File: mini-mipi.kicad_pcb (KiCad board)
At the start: 4 copper layers, 43.2 x 34.9 mm, 56 parts, among them IC1 ECP5-BGA256, J1 Conn_ARM_JTAG_SWD_10, J2 Conn_01x15, J3 USB_B_Micro, J4 Micro_SD_Card, U1 TPS74633, U2 TPS74618, U3 TPS74625, U4 TPS74611, U5 AT25SF081-SSHD-X, U6 S27KL0641, U7 OSC_25M

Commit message: Add semi-critical resistor values
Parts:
- R1, R2, R3: value R -> 10k
- R12, R13, R14, R15, R17, R18: value R -> 4.7k
- R16: value R -> 1k
- R6: value R -> 15k
- R7, R8: value R_Small -> 0
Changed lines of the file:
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@@
-(kicad_pcb (version 20200628) (host pcbnew "5.99.0-unknown-7340c97~102~ubuntu20.04.1")
+(kicad_pcb (version 20200628) (host pcbnew "5.99.0-unknown-e9da02e~102~ubuntu20.04.1")
   (general
     (thickness 1.6)
@@
       (effects (font (size 1 1) (thickness 0.15)))
     )
-    (fp_text value "R" (at 0 1.17) (layer "F.Fab")
+    (fp_text value "4.7k" (at 0 1.17) (layer "F.Fab")
       (effects (font (size 1 1) (thickness 0.15)))
     )
@@
       (effects (font (size 1 1) (thickness 0.15)) (justify mirror))
     )
-    (fp_text value "R" (at 0 -1.17) (layer "B.Fab")
+    (fp_text value "4.7k" (at 0 -1.17) (layer "B.Fab")
       (effects (font (size 1 1) (thickness 0.15)) (justify mirror))
     )
@@
       (effects (font (size 1 1) (thickness 0.15)) (justify mirror))
     )
-    (fp_text value "R" (at 0 -1.17) (layer "B.Fab")
+    (fp_text value "1k" (at 0 -1.17) (layer "B.Fab")
       (effects (font (size 1 1) (thickness 0.15)) (justify mirror))
     )
@@
       (effects (font (size 1 1) (thickness 0.15)) (justify mirror))
     )
-    (fp_text value "R" (at 0 -1.17) (layer "B.Fab")
+    (fp_text value "4.7k" (at 0 -1.17) (layer "B.Fab")
       (effects (font (size 1 1) (thickness 0.15)) (justify mirror))
     )
@@
       (effects (font (size 1 1) (thickness 0.15)) (justify mirror))
     )
-    (fp_text value "R" (at 0 -1.17) (layer "B.Fab")
+    (fp_text value "4.7k" (at 0 -1.17) (layer "B.Fab")
       (effects (font (size 1 1) (thickness 0.15)) (justify mirror))
     )
@@
       (effects (font (size 1 1) (thickness 0.15)) (justify mirror))
     )
-    (fp_text value "R" (at 0 -1.17) (layer "B.Fab")
+    (fp_text value "4.7k" (at 0 -1.17) (layer "B.Fab")
       (effects (font (size 1 1) (thickness 0.15)) (justify mirror))
     )
@@
       (effects (font (size 1 1) (thickness 0.15)) (justify mirror))
     )
-    (fp_text value "R" (at 0 -1.17) (layer "B.Fab")
+    (fp_text value "4.7k" (at 0 -1.17) (layer "B.Fab")
       (effects (font (size 1 1) (thickness 0.15)) (justify mirror))
     )
@@
       (effects (font (size 1 1) (thickness 0.15)))
     )
-    (fp_text value "R_Small" (at 0 1.17 90) (layer "F.Fab")
+    (fp_text value "0" (at 0 1.17 90) (layer "F.Fab")
       (effects (font (size 1 1) (thickness 0.15)))
     )
@@
       (effects (font (size 1 1) (thickness 0.15)))
     )
-    (fp_text value "R_Small" (at 0 1.17 90) (layer "F.Fab")
+    (fp_text value "0" (at 0 1.17 90) (layer "F.Fab")
       (effects (font (size 1 1) (thickness 0.15)))
     )
@@
       (effects (font (size 1 1) (thickness 0.15)))
     )
-    (fp_text value "R" (at 0 1.17 90) (layer "F.Fab")
+    (fp_text value "15k" (at 0 1.17 90) (layer "F.Fab")
       (effects (font (size 1 1) (thickness 0.15)))
     )
@@
       (effects (font (size 1 1) (thickness 0.15)) (justify mirror))
     )
-    (fp_text value "R" (at 0 -1.17 90) (layer "B.Fab")
+    (fp_text value "10k" (at 0 -1.17 90) (layer "B.Fab")
       (effects (font (size 1 1) (thickness 0.15)) (justify mirror))
     )
@@
       (effects (font (size 1 1) (thickness 0.15)) (justify mirror))
     )
-    (fp_text value "R" (at 0 -1.17 90) (layer "B.Fab")
+    (fp_text value "10k" (at 0 -1.17 90) (layer "B.Fab")
       (effects (font (size 1 1) (thickness 0.15)) (justify mirror))
     )
@@
       (effects (font (size 1 1) (thickness 0.15)) (justify mirror))
     )
-    (fp_text value "R" (at 0 -1.17 90) (layer "B.Fab")
-      (effects (font (size 1 1) (thickness 0.15)) (justify mirror))
-    )
+    (fp_text value "10k" (at 0 -1.17 90) (layer "B.Fab")
+      (effects (font (size 1 1) (thickness 0.15)) (justify mirror))
+    )

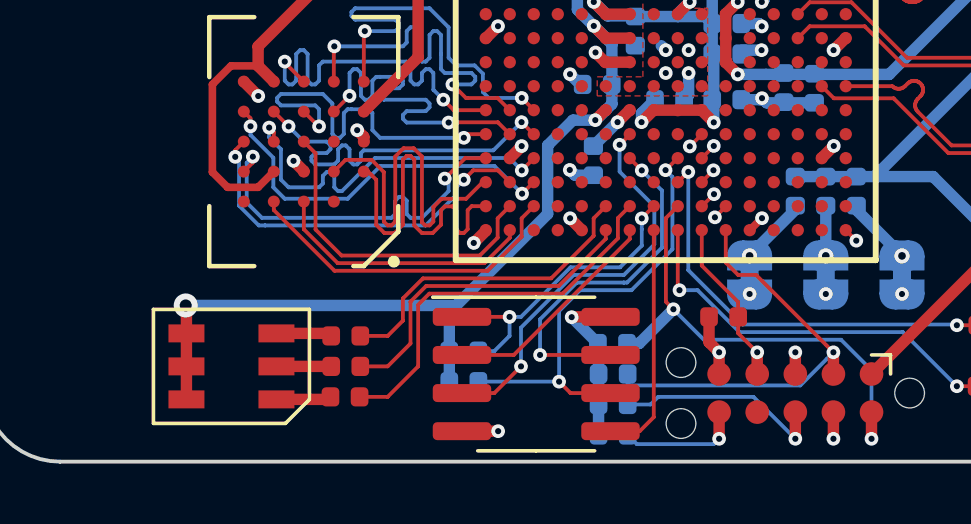
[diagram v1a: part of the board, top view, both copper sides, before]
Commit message: Add more pullup resistors
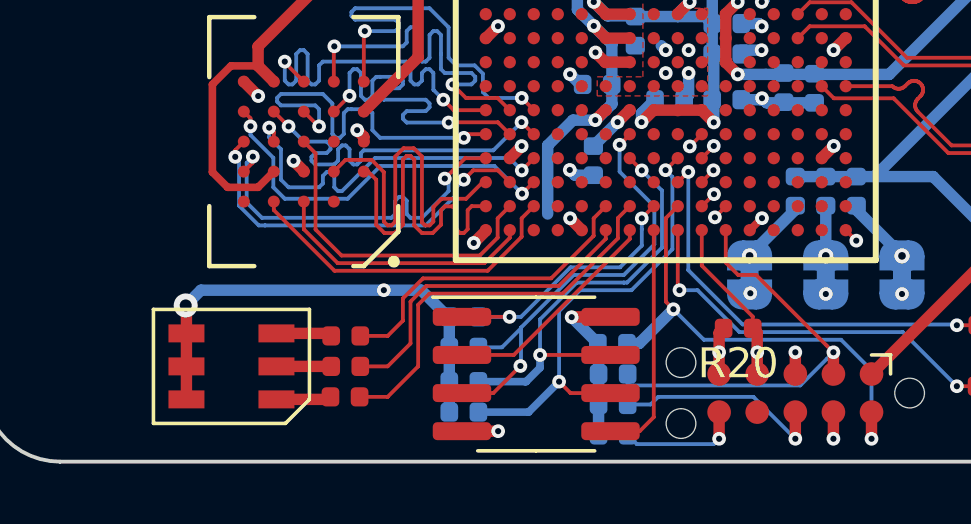
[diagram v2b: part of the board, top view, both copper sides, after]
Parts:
- added R19: 4.7k, Resistor_SMD:R_0402_1005Metric, B.Cu at (157.6, 94.5)
- added R20: 4.7k, Resistor_SMD:R_0402_1005Metric, F.Cu at (166.8, 92.7)
- R18: moved to B.Cu
- moved R18 8.72 mm to (157.6, 93.3)
- moved R17 1.14 mm to (157.6, 92.3)
- moved R16 1.02 mm to (157.6, 95.5)
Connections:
- R18 pad 1: GND -> VCC
- R18 pad 2: /CONFIG/TCK -> /CONFIG/DIO2
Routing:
- net VCC: track 127.6 -> 130.8 mm, vias 14 -> 15
- net /CONFIG/DIO3: track 12.0 -> 14.7 mm
- net /CONFIG/DIO2: track 13.5 -> 15.2 mm
- net /CONFIG/CSN: track 10.3 -> 9.50 mm

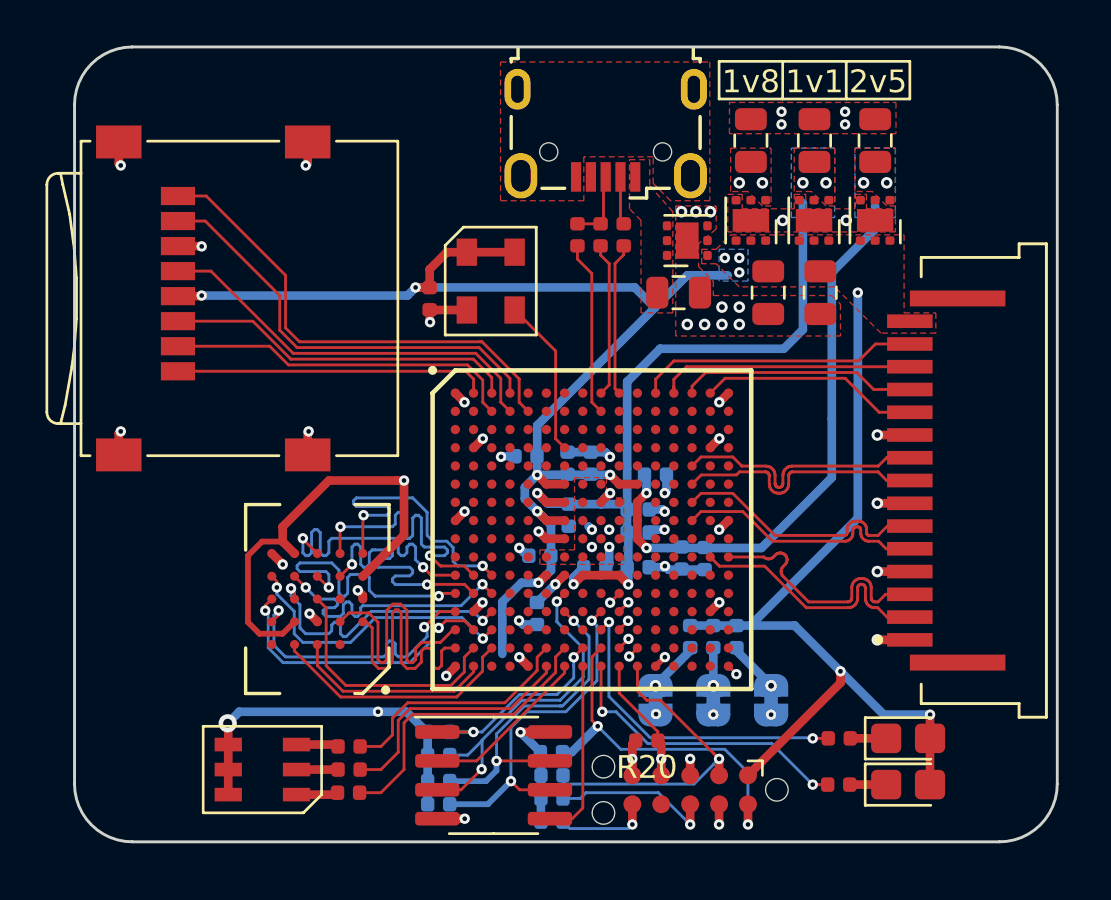
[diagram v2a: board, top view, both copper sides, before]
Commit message: Change oscillator to SI5315, change RGB LED
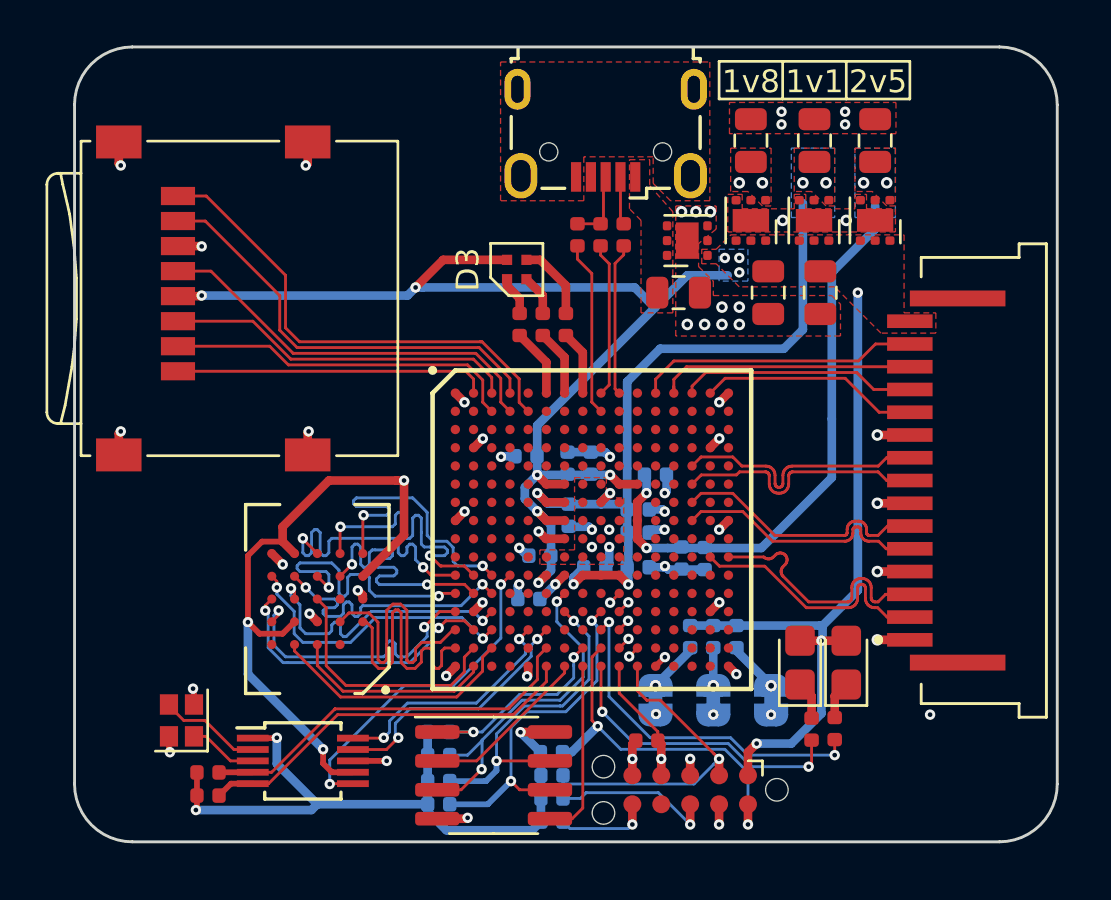
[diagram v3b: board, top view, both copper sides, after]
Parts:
- removed C1: C, Capacitor_SMD:C_0402_1005Metric
- added R21: R, Resistor_SMD:R_0402_1005Metric, F.Cu at (147.5, 94.1)
- added R22: R, Resistor_SMD:R_0402_1005Metric, F.Cu at (147.5, 95.1)
- added Y1: Crystal_GND24, Crystal:Crystal_SMD_2016-4Pin_2.0x1.6mm, F.Cu at (146.3, 91.8)
- D3: value LED_RGB -> LED_RGBA; footprint mini-mipi:FM-Z3535RGBA-SH -> mini-mipi:LED_0404
- U7: value OSC_25M -> SI5351A-B-GTR; footprint mini-mipi:SOIC-4 -> Package_SO:MSOP-10_3x3mm_P0.5mm
- moved D3 24.7 mm to (161.0, 72.0), turned to 0 degrees
- moved R11 22.7 mm to (163.2, 74.4), turned to -90 degrees
- moved U7 22.6 mm to (151.6, 93.6), turned to 0 degrees
- moved R10 21.3 mm to (162.2, 74.4), turned to -90 degrees
- moved R9 20.0 mm to (161.2, 74.4), turned to -90 degrees
- moved D1 7.16 mm to (173.5, 89.3), turned to 90 degrees
- moved D2 4.30 mm to (175.5, 89.3), turned to 90 degrees
- moved R4 2.71 mm to (174.0, 92.2), turned to 90 degrees
- moved C14 0.73 mm to (161.6, 86.5), turned to 180 degrees
- moved R5 0.47 mm to (175.0, 92.2), turned to 90 degrees
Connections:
- IC1 pad B1: Net-(IC1-PadB1) -> (no net)
- IC1 pad B2: Net-(IC1-PadB2) -> (no net)
- IC1 pad C1: Net-(IC1-PadC1) -> (no net)
- IC1 pad C2: Net-(IC1-PadC2) -> (no net)
- IC1 pad C3: Net-(IC1-PadC3) -> (no net)
- IC1 pad D1: Net-(IC1-PadD1) -> (no net)
- IC1 pad D3: Net-(IC1-PadD3) -> (no net)
- IC1 pad E1: Net-(IC1-PadE1) -> (no net)
- IC1 pad E2: Net-(IC1-PadE2) -> (no net)
- IC1 pad E3: Net-(IC1-PadE3) -> (no net)
- IC1 pad F1: Net-(IC1-PadF1) -> (no net)
- IC1 pad F2: Net-(IC1-PadF2) -> (no net)
- IC1 pad F3: Net-(IC1-PadF3) -> (no net)
- IC1 pad F4: Net-(IC1-PadF4) -> (no net)
- IC1 pad F5: Net-(IC1-PadF5) -> (no net)
- IC1 pad G1: Net-(IC1-PadG1) -> (no net)
- IC1 pad G2: Net-(IC1-PadG2) -> (no net)
- IC1 pad G3: Net-(IC1-PadG3) -> (no net)
- IC1 pad G4: Net-(IC1-PadG4) -> (no net)
- IC1 pad G5: Net-(IC1-PadG5) -> (no net)
- IC1 pad H2: Net-(IC1-PadH2) -> (no net)
- IC1 pad H3: Net-(IC1-PadH3) -> (no net)
- IC1 pad H4: Net-(IC1-PadH4) -> (no net)
- IC1 pad H5: Net-(IC1-PadH5) -> (no net)
- IC1 pad H6: VCC -> (no net)
- IC1 pad H7: VCC -> (no net)
- IC1 pad J1: Net-(IC1-PadJ1) -> (no net)
- IC1 pad J2: Net-(IC1-PadJ2) -> (no net)
- IC1 pad J3: Net-(IC1-PadJ3) -> (no net)
- IC1 pad J4: Net-(IC1-PadJ4) -> (no net)
- IC1 pad J5: Net-(IC1-PadJ5) -> (no net)
- IC1 pad K1: Net-(IC1-PadK1) -> (no net)
- IC1 pad K2: Net-(IC1-PadK2) -> (no net)
- IC1 pad K3: Net-(IC1-PadK3) -> (no net)
- IC1 pad R6: Net-(IC1-PadR6) -> OSC_SDA
- IC1 pad T6: Net-(IC1-PadT6) -> OSC_SCL
- R10 pad 2: Net-(IC1-PadT6) -> Net-(IC1-PadA7)
- R11 pad 1: Net-(D3-Pad1) -> Net-(D3-Pad3)
- R11 pad 2: Net-(IC1-PadR7) -> Net-(IC1-PadA8)
- R9 pad 1: Net-(D3-Pad3) -> Net-(D3-Pad1)
- R9 pad 2: Net-(IC1-PadR6) -> Net-(IC1-PadA6)
- U7 pad 2: GND -> /MEMORY/OSC_XA
- U7 pad 3: Net-(IC1-PadD7) -> /MEMORY/OSC_XB
- U7 pad 4: VCC -> OSC_SDA
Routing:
- net OSC_SDA: track 0.00 -> 17.2 mm
- net OSC_SCL: track 0.00 -> 17.1 mm
- net Net-(IC1-PadL4): track 0.00 -> 14.7 mm, vias 0 -> 2
- net Net-(IC1-PadR7): track 13.2 -> 0.00 mm
- net Net-(IC1-PadP6): track 0.00 -> 11.5 mm, vias 0 -> 2
- net Net-(IC1-PadT6): track 11.1 -> 0.00 mm
- net Net-(IC1-PadR6): track 10.8 -> 0.00 mm
- net Net-(IC1-PadP5): track 0.00 -> 10.7 mm, vias 0 -> 2
- net +1V8: track 50.1 -> 59.0 mm, vias 4 -> 6
- net VCC: track 130.8 -> 123.5 mm, vias 15 -> 16
- net Net-(IC1-PadD7): track 6.96 -> 0.00 mm
- net /MEMORY/OSC_XA: track 0.00 -> 4.53 mm
- net /MEMORY/OSC_XB: track 0.00 -> 3.03 mm
- net Net-(IC1-PadA6): track 0.00 -> 3.02 mm
- net Net-(IC1-PadA7): track 0.00 -> 2.93 mm
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
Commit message: Change 1.8v and 3.3v regulators to buck for #2
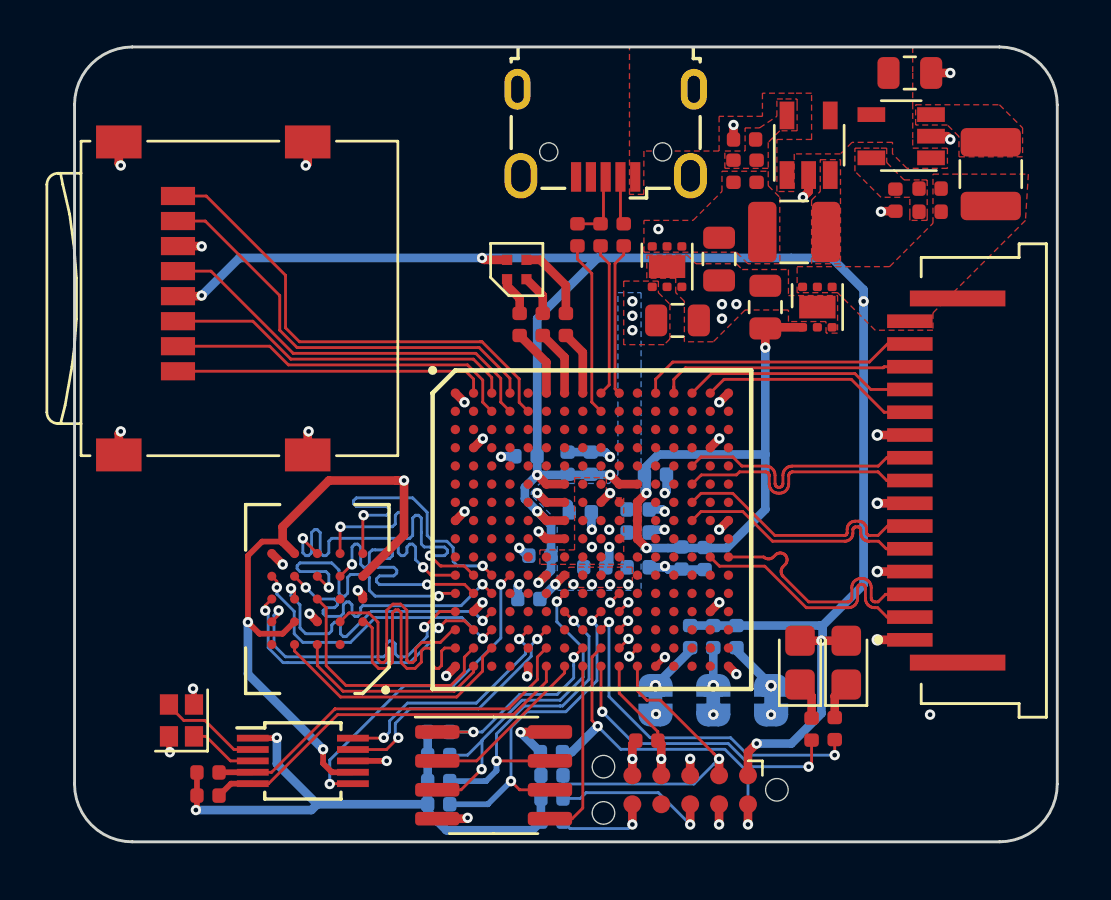
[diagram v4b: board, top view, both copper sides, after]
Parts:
- removed C2: C, Capacitor_SMD:C_0805_2012Metric
- added C21: C, Capacitor_SMD:C_0402_1005Metric, F.Cu at (170.6, 67.7)
- added L1: L, Inductor_SMD:L_1210_3225Metric, F.Cu at (181.9, 67.8)
- added L3: L, Inductor_SMD:L_1210_3225Metric, F.Cu at (173.2, 70.4)
- added R23: R, Resistor_SMD:R_0402_1005Metric, F.Cu at (179.2, 68.5)
- added R24: R, Resistor_SMD:R_0402_1005Metric, F.Cu at (177.7, 69.0)
- added R27: R, Resistor_SMD:R_0402_1005Metric, F.Cu at (171.6, 67.7)
- added R28: R, Resistor_SMD:R_0402_1005Metric, F.Cu at (171.0, 66.3)
- C4: footprint Capacitor_SMD:C_0805_2012Metric -> Capacitor_SMD:C_0402_1005Metric
- U1: value TPS74633 -> AP3429-A; footprint Package_SON:WSON-6-1EP_2x2mm_P0.65mm_EP1x1.6mm -> Package_TO_SOT_SMD:TSOT-23-5
- U2: value TPS74618 -> TPS74625
- U3: value TPS74625 -> AP3429-A; footprint Package_SON:WSON-6-1EP_2x2mm_P0.65mm_EP1x1.6mm -> Package_TO_SOT_SMD:TSOT-23-5
- moved U1 10.5 mm to (177.9, 66.2)
- moved C3 10.4 mm to (178.3, 63.4), turned to 0 degrees
- moved C8 9.93 mm to (168.1, 74.2), turned to 0 degrees
- moved C7 8.77 mm to (172.0, 73.7)
- moved C4 8.47 mm to (179.2, 69.5), turned to 180 degrees
- moved U4 6.77 mm to (167.6, 71.9), turned to 90 degrees
- moved U2 4.80 mm to (174.2, 73.7), turned to 90 degrees
- moved U3 4.41 mm to (173.9, 66.5), turned to 90 degrees
- moved C20 2.31 mm to (169.9, 71.5), turned to -90 degrees
- moved C11 0.52 mm to (163.8, 82.7), turned to 0 degrees
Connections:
- C20 pad 1: VBUS -> +1V8
- C3 pad 1: VCC -> VBUS
- C4 pad 1: +1V8 -> VCC
- C4 pad 2: GND -> Net-(C4-Pad2)
- U1 pad 1: VCC -> VBUS
- U1 pad 2: Net-(U1-Pad2) -> GND
- U1 pad 3: GND -> Net-(L1-Pad1)
- U1 pad 5: Net-(U1-Pad5) -> Net-(C4-Pad2)
- U2 pad 1: +1V8 -> +2V5
- U3 pad 1: +2V5 -> VBUS
- U3 pad 2: Net-(U3-Pad2) -> GND
- U3 pad 3: GND -> Net-(L3-Pad1)
- U3 pad 4: VCC -> VBUS
- U4 pad 4: VCC -> +1V8
- U4 pad 6: VCC -> +1V8
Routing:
- net +1V1: track 33.6 -> 2.00 mm, vias 6 -> 9
- net VCC: track 123.5 -> 127.6 mm, vias 16 -> 13
- net +1V8: track 59.0 -> 55.1 mm, vias 6 -> 5
- net GND: track 37.5 -> 41.3 mm, vias 61 -> 54
- net +2V5: track 32.0 -> 31.2 mm, vias 5 -> 4
- added copper zone on F.Cu, net Net-(C21-Pad2)
- added copper zone on F.Cu, net Net-(C4-Pad2)
- added copper zone on F.Cu, net Net-(L1-Pad1)
- added copper zone on F.Cu, net Net-(L3-Pad1)
- removed copper zone on In1.Cu, net +1V8
- removed copper zone on B.Cu, net +2V5
- removed copper zone on F.Cu, net +2V5
- removed copper zone on B.Cu, net VCC
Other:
- board text removed: "1v1"
- board text removed: "1v8"
- board text removed: "2v5"

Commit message: Improve decoupling
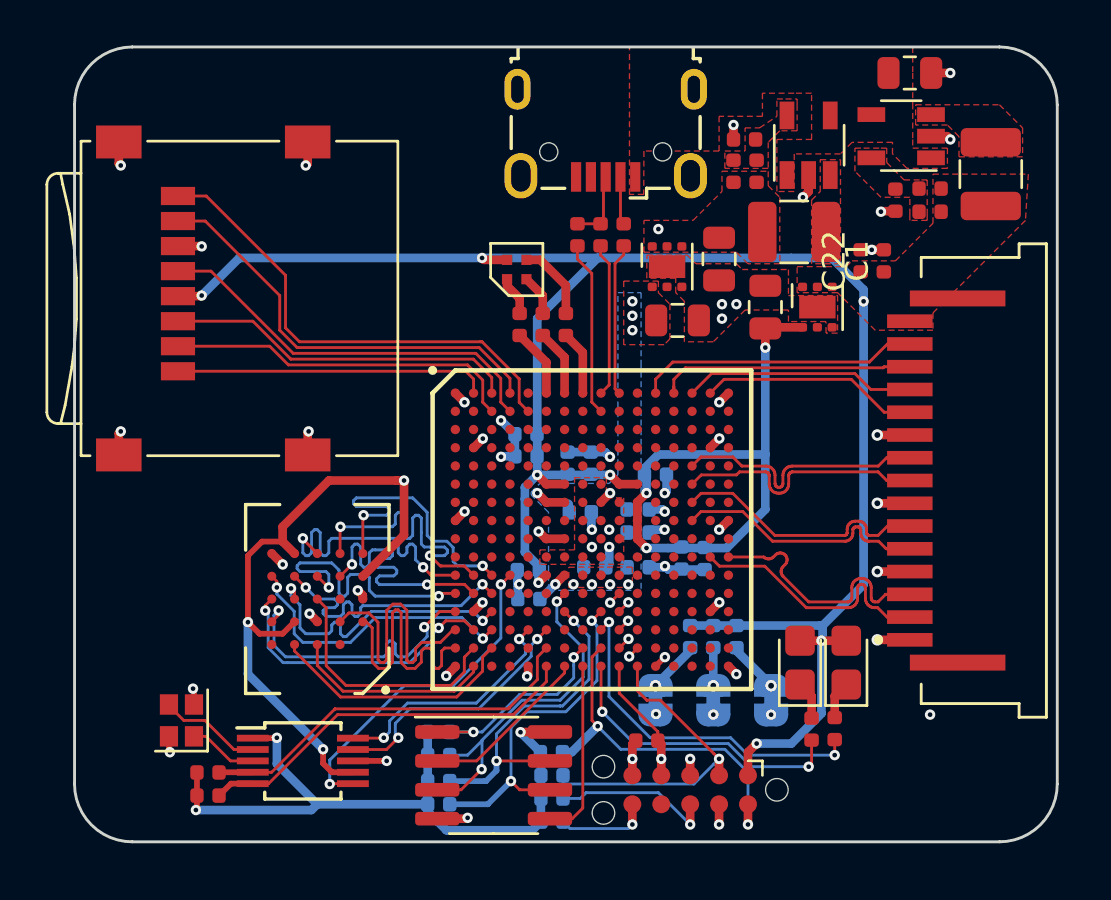
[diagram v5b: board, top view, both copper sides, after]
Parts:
- added C1: C, Capacitor_SMD:C_0402_1005Metric, F.Cu at (177.2, 71.6)
- added C2: C, Capacitor_SMD:C_0402_1005Metric, B.Cu at (161.5, 85.2)
- added C22: C, Capacitor_SMD:C_0402_1005Metric, F.Cu at (176.1, 71.6)
- moved C5 5.37 mm to (161.4, 79.2)
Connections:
- U2 pad 4: VCC -> Net-(U2-Pad4)
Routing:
- net GND: track 41.3 -> 44.2 mm, vias 54 -> 55
- net VCC: track 127.6 -> 125.8 mm, vias 13 -> 12
